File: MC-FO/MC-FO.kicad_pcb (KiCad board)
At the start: 4 copper layers, 160 x 100 mm, 102 parts, among them U101 74ACT08SCX, U102 IFE98, U11 74LVCE1G08W5-7, U121 74ACT08SCX, U122 IFE98, U141 IFD97, U142 74LVC1G02SE-7, U161 IFD97, U162 74LVC1G02SE-7, U181 74LVC1G07QDCKTQ1, U182 74LVCE1G08W5-7, U183 BU4831F-TR, U184 BU4847F-TR, U2 R-78E3.3-0.5, U21 74ACT08SCX, U22 IFE98, U3 R-78E5.0-0.5, U41 74ACT08SCX, U42 IFE98, U61 74ACT08SCX, U62 IFE98, U81 74ACT08SCX, U82 IFE98

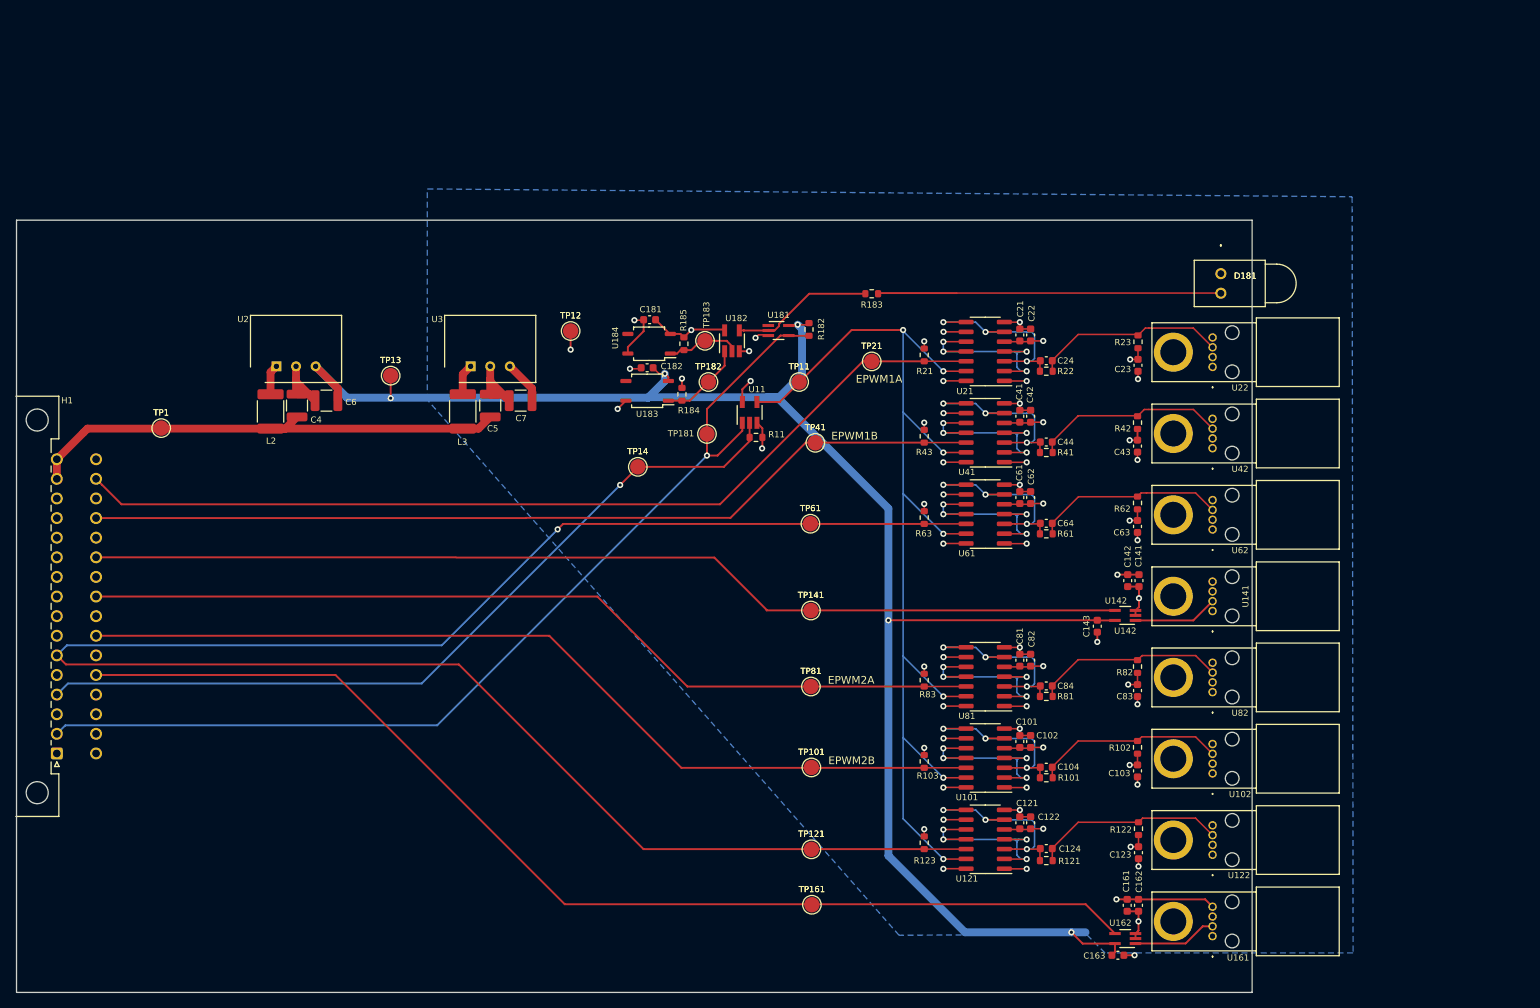
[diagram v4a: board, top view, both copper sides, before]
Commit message: simplify vias, mechanical hole change
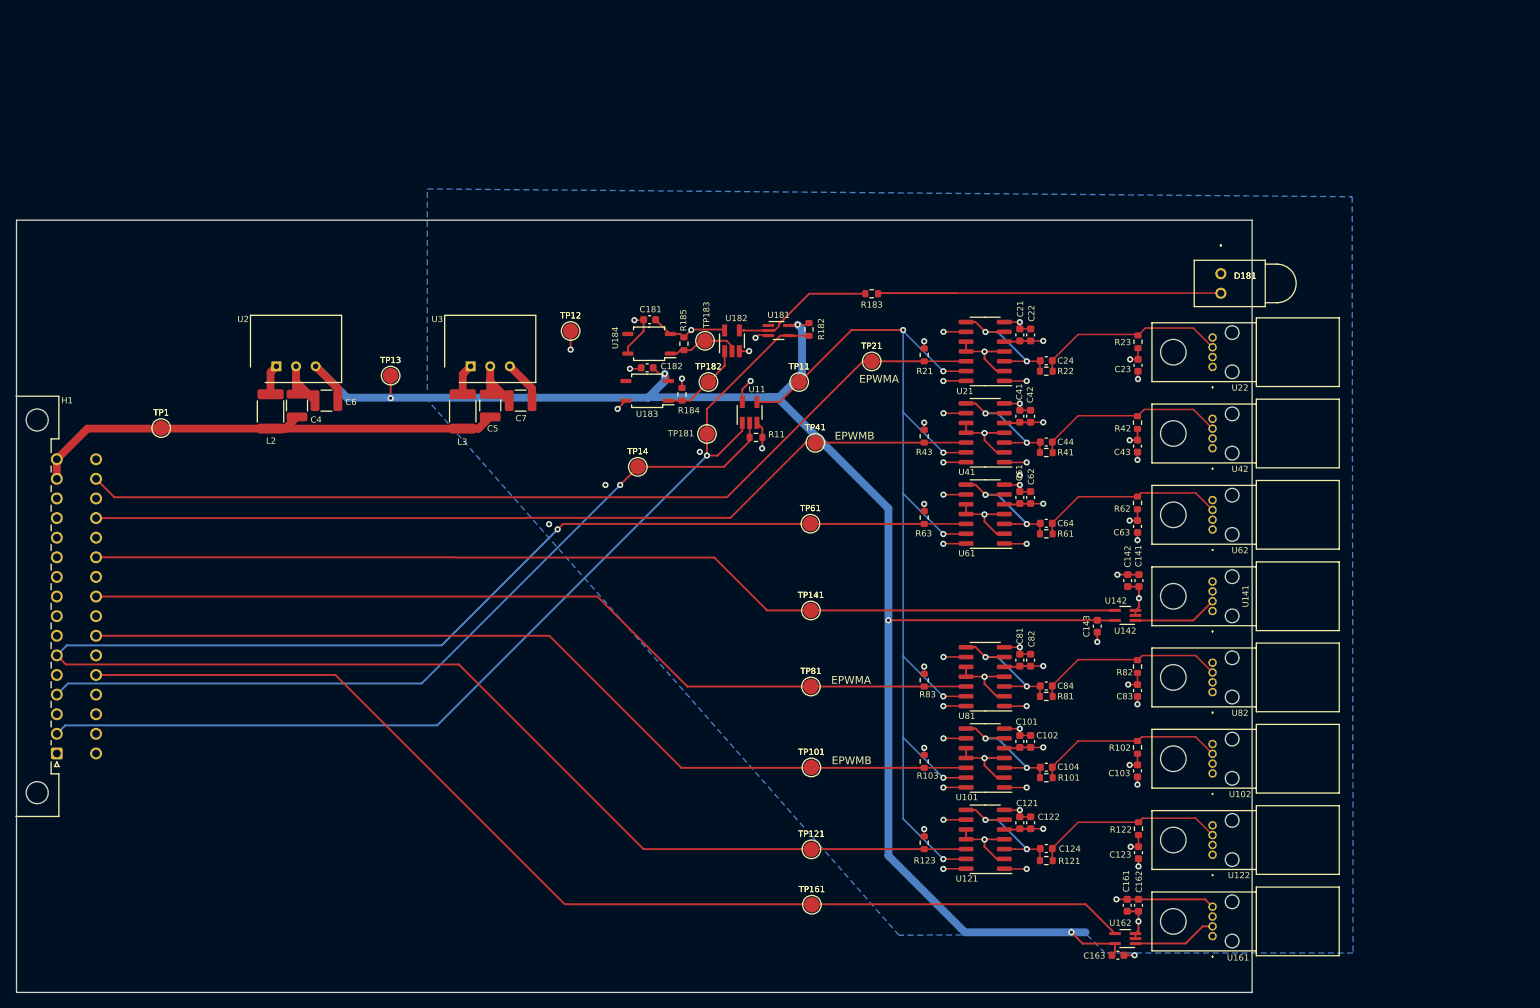
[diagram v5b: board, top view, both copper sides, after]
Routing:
- net Net-(U101-Pad10): track 27.8 -> 10.4 mm, vias 4 -> 1
- net Net-(U81-Pad10): track 27.8 -> 10.4 mm, vias 4 -> 1
- net Net-(U61-Pad10): track 27.8 -> 10.4 mm, vias 4 -> 1
- net Net-(U41-Pad10): track 27.8 -> 10.4 mm, vias 4 -> 1
- net Net-(U21-Pad10): track 27.8 -> 10.4 mm, vias 4 -> 1
- net Net-(U121-Pad10): track 27.8 -> 10.4 mm, vias 4 -> 1
- net Net-(C124-Pad1): track 29.4 -> 19.5 mm, vias 3 -> 2
- net Net-(C64-Pad1): track 29.1 -> 19.5 mm, vias 3 -> 2
- net Net-(C104-Pad1): track 29.1 -> 19.5 mm, vias 3 -> 2
- net Net-(C84-Pad1): track 29.1 -> 19.5 mm, vias 3 -> 2
- net Net-(C24-Pad1): track 29.1 -> 19.5 mm, vias 3 -> 2
- net Net-(C44-Pad1): track 29.1 -> 19.5 mm, vias 3 -> 2
- net /Detector1/5V: track 137.4 -> 139.9 mm
- net EPWM1A: track 121.7 -> 120.9 mm
- net GND: vias 28 -> 31
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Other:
- board text added: "EPWMA"
- board text added: "EPWMB"
- board text removed: "EPWM1A"
- board text removed: "EPWM1B"
- board text removed: "EPWM2A"
- board text removed: "EPWM2B"
- board text removed: "EPWMA1"

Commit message: Add files via upload
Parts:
- moved R11 13.6 mm to (193.4, 71.3)
- moved U11 13.6 mm to (192.5, 68.1)
- moved TP11 11.5 mm to (197.0, 65.0)
- moved TP181 5.15 mm to (180.9, 78.6)
- moved TP41 3.81 mm to (193.6, 79.6)
- moved TP21 2.86 mm to (200.0, 69.2)
- moved C163 1.05 mm to (229.4, 145.0)
- moved U162 0.72 mm to (229.9, 143.1)
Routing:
- net /Emitter1/RESET_FO: track 147.7 -> 133.3 mm
- net EMITTER_ENABLE: track 105.7 -> 119.8 mm
- net /Detector1/5V: track 139.9 -> 138.3 mm
- net ~SAFE_STATE_FLAG~: track 129.2 -> 128.0 mm
- net GND: track 97.4 -> 98.5 mm
- net (no net): vias 1 -> 0
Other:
- board text added: "24V"
- board text added: "3V3"
- board text added: "3V3_monitor"
- board text added: "5V"
- board text added: "5V_monitor"
- board text added: "EMITTER_ENABLE"
- board text added: "RESET_FO"
- board text added: "SAFE STATE LED INDICATOR"
- board text added: "SAFE_STATE_FLAG"
- board text added: "Status2"

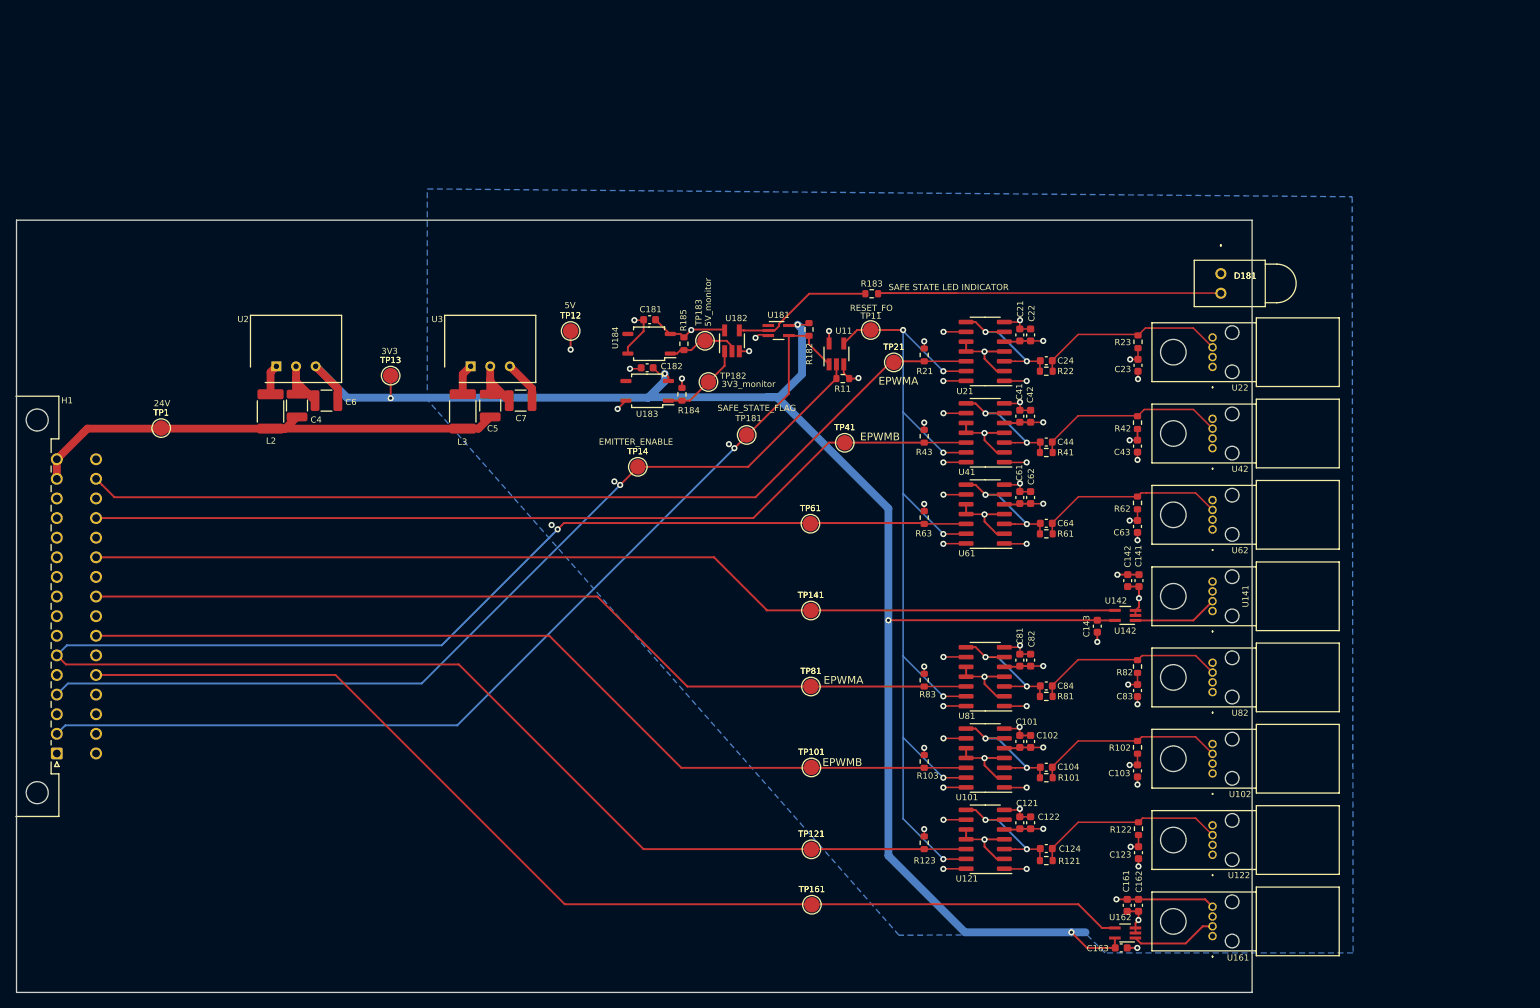
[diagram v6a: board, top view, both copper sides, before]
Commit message: Layout Revision
-removed MH1 from emitter/detector symbol
-pin out changes to assist with routing on the backplane
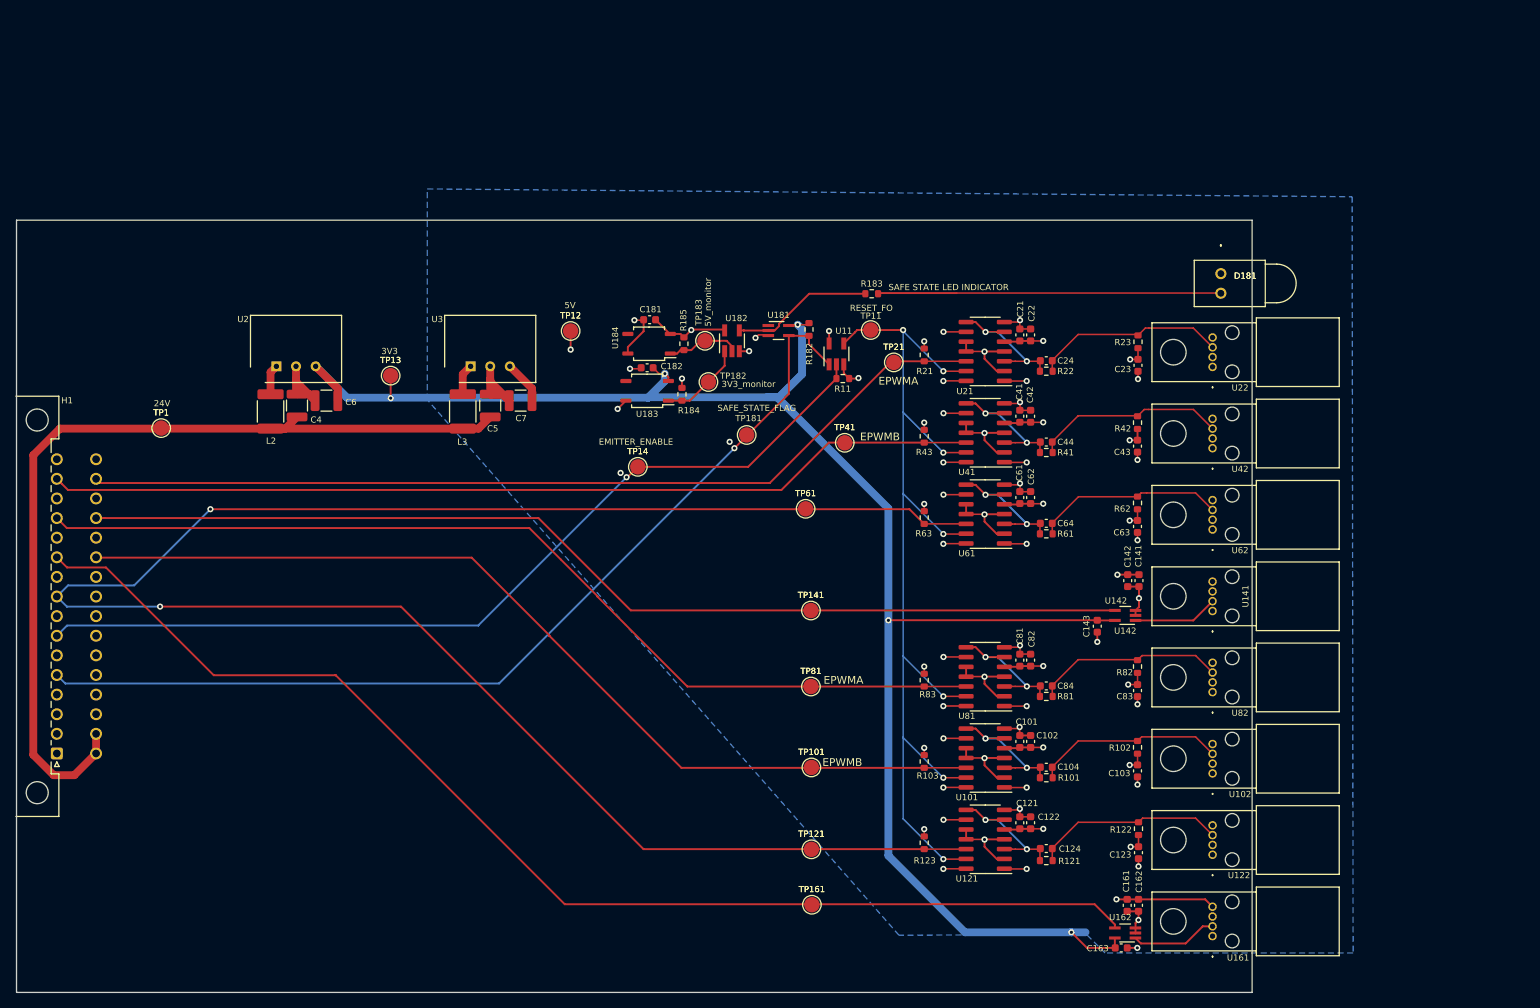
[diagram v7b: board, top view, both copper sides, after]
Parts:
- moved TP61 2.03 mm to (188.5, 88.2)
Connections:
- H1 pad 11: GND -> STATUS2
- H1 pad 13: GND -> EPWM2A
- H1 pad 15: 24V -> EPWM1B
- H1 pad 16: 24V -> GND
- H1 pad 17: GND -> 24V
- H1 pad 18: GND -> 24V
- H1 pad 2: ~SAFE_STATE_FLAG~ -> GND
- H1 pad 21: STATUS2 -> GND
- H1 pad 23: EPWM2B -> GND
- H1 pad 25: EPWM2A -> GND
- H1 pad 27: STATUS1 -> EPWM2B
- H1 pad 29: EPWM1B -> STATUS1
- H1 pad 4: EMITTER_ENABLE -> GND
- H1 pad 5: GND -> ~SAFE_STATE_FLAG~
- H1 pad 6: RESET_GPIO -> GND
- H1 pad 7: GND -> EMITTER_ENABLE
- H1 pad 9: GND -> RESET_GPIO
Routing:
- net 24V: track 63.1 -> 115.6 mm
- net STATUS2: track 145.5 -> 157.2 mm
- net EPWM2A: track 117.5 -> 126.8 mm
- net EPWM2B: track 119.8 -> 124.0 mm
- net EPWM1B: track 116.7 -> 120.9 mm
- net EMITTER_ENABLE: track 119.8 -> 116.5 mm
- net ~SAFE_STATE_FLAG~: track 128.0 -> 125.7 mm
- net STATUS1: track 134.8 -> 136.9 mm
- net EPWM1A: track 120.9 -> 119.4 mm
- net RESET_GPIO: track 253.1 -> 254.5 mm, vias 1 -> 2
- net GND: vias 31 -> 30

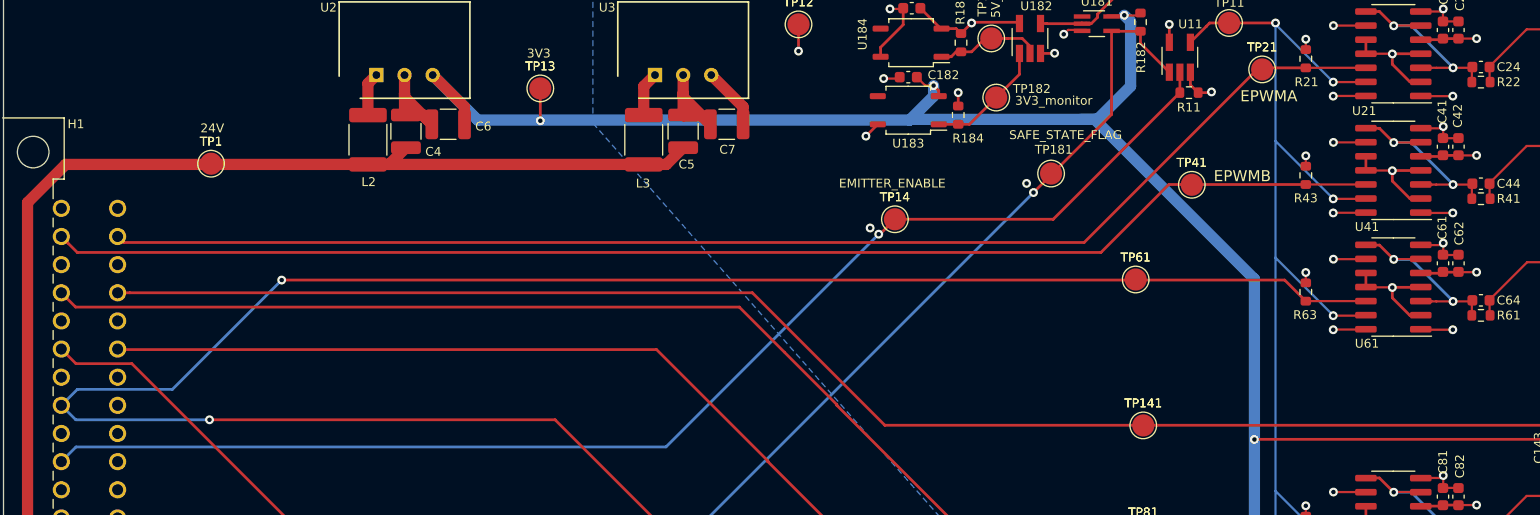
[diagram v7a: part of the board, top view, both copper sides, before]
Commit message: some DRC edits and pinout changes
still need to:
- add gnd test points 
- fix pad too close to pad errors
- spread the reference vias on the traces that change layers farther apart
-allow more layout around U2 and U3 in the layout due to 24V
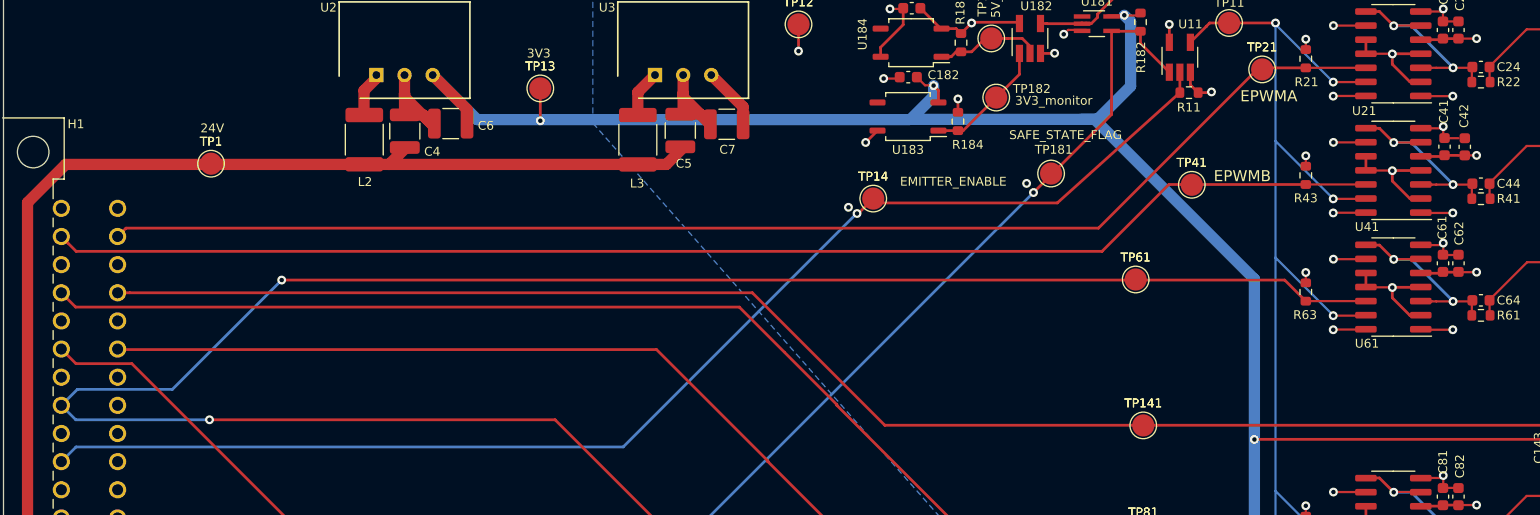
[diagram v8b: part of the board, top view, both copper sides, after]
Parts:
- moved TP14 2.70 mm to (164.9, 80.9)
- moved R184 0.57 mm to (172.5, 73.9)
- moved U183 0.57 mm to (168.0, 73.5)
- moved C42 0.57 mm to (218.2, 76.2)
- moved L3 0.53 mm to (143.6, 75.6)
- moved L2 0.33 mm to (118.9, 75.6)
- moved C5 0.27 mm to (147.4, 74.7)
- moved C6 0.24 mm to (126.7, 74.1)
- moved C41 0.14 mm to (216.4, 76.2)
- moved C4 0.10 mm to (122.6, 74.8)
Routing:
- net GND: track 98.5 -> 99.1 mm
